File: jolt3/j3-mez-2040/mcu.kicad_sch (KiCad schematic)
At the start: 21 parts, among them SW2 SW_SPST, U1 RP2040, Y1 ABM8-272-T3

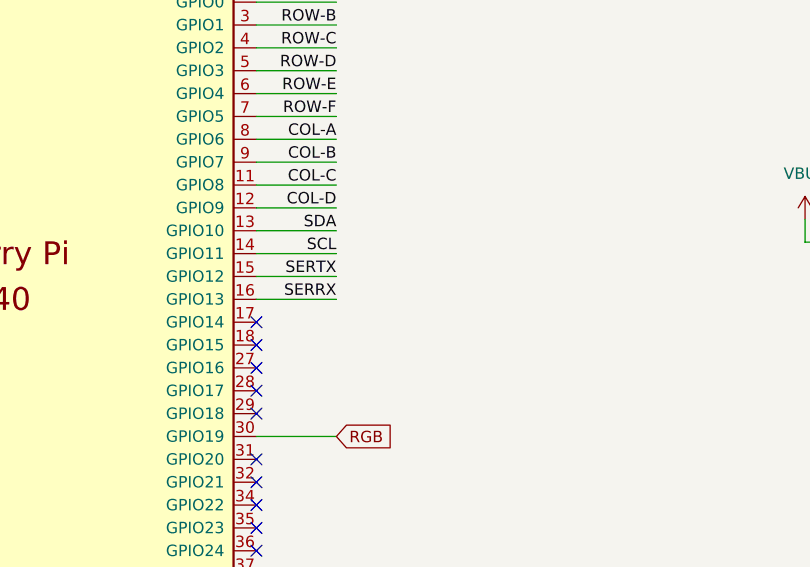
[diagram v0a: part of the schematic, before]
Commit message: Jolt 3: Rev A for 3 boards
Send Rev A out for jolt3-left, jolt3-right, and j3-mez-2040.
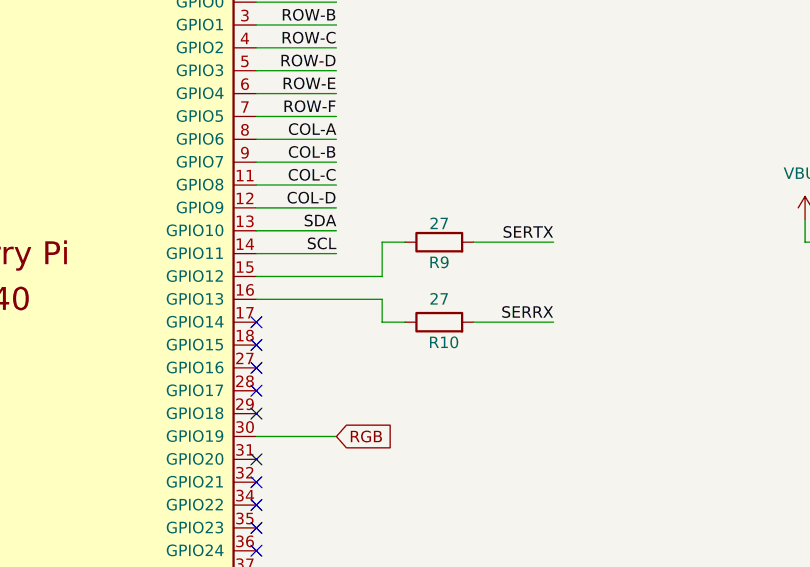
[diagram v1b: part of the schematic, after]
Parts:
- added R10, R9: 27, Resistor_SMD:R_0402_1005Metric, symbol Device:R
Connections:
- net SERRX: now also R10.2; no longer U1.16 (GPIO13)
- net SERTX: now also R9.2; no longer U1.15 (GPIO12)
- new net: R10.1, U1.16 (GPIO13)
- new net: R9.1, U1.15 (GPIO12)
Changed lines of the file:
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@@
+	(wire
+		(pts
+			(xy 146.05 134.62) (xy 148.59 134.62)
+		)
+		(stroke
+			(width 0)
+			(type default)
+		)
+	)
 	(wire
 		(pts
@@
 	(wire
 		(pts
-			(xy 132.08 138.43) (xy 140.97 138.43)
+			(xy 132.08 138.43) (xy 146.05 138.43)
 		)
 		(stroke
@@
 	(wire
 		(pts
+			(xy 146.05 143.51) (xy 148.59 143.51)
+		)
+		(stroke
+			(width 0)
+			(type default)
+		)
+	)
+	(wire
+		(pts
 			(xy 204.47 33.02) (xy 204.47 34.29)
 		)
@@
 	(wire
 		(pts
+			(xy 146.05 140.97) (xy 146.05 143.51)
+		)
+		(stroke
+			(width 0)
+			(type default)
+		)
+	)
+	(wire
+		(pts
 			(xy 116.84 33.02) (xy 116.84 52.07)
 		)
@@
 	(wire
 		(pts
+			(xy 146.05 138.43) (xy 146.05 134.62)
+		)
+		(stroke
+			(width 0)
+			(type default)
+		)
+	)
+	(wire
+		(pts
 			(xy 179.07 41.91) (xy 179.07 44.45)
 		)
@@
 	(wire
 		(pts
+			(xy 156.21 143.51) (xy 165.1 143.51)
+		)
+		(stroke
+			(width 0)
+			(type default)
+		)
+	)
+	(wire
+		(pts
 			(xy 116.84 63.5) (xy 116.84 90.17)
 		)
@@
 	(wire
 		(pts
-			(xy 132.08 140.97) (xy 140.97 140.97)
+			(xy 132.08 140.97) (xy 146.05 140.97)
 		)
 		(stroke
@@
 		(pts
 			(xy 132.08 113.03) (xy 140.97 113.03)
+		)
+		(stroke
+			(width 0)
+			(type default)
+		)
+	)
+	(wire
+		(pts
+			(xy 156.21 134.62) (xy 165.1 134.62)
 		)
 		(stroke
@@
 	)
 	(label "SERTX"
-		(at 140.97 138.43 180)
+		(at 165.1 134.62 180)
 		(effects
 			(font
@@
 	)
 	(label "SERRX"
-		(at 140.97 140.97 180)
+		(at 165.1 143.51 180)
 		(effects
 			(font
@@
 		)
 	)
+	(symbol
+		(lib_id "Device:R")
+		(at 152.4 143.51 90)
+		(unit 1)
+		(exclude_from_sim no)
+		(in_bom yes)
+		(on_board yes)
+		(dnp no)
+		(property "Reference" "R10"
+			(at 152.908 145.796 90)
+			(effects
+				(font
+					(size 1.27 1.27)
+				)
+			)
+		)
+		(property "Value" "27"
+			(at 152.4 140.97 90)
+			(effects
+				(font
+					(size 1.27 1.27)
+				)
+			)
+		)
+		(property "Footprint" "Resistor_SMD:R_0402_1005Metric"
+			(at 152.4 145.288 90)
+			(effects
+				(font
+					(size 1.27 1.27)
+				)
+				(hide yes)
+			)
+		)
+		(property "Datasheet" "~"
+			(at 152.4 143.51 0)
+			(effects
+				(font
+					(size 1.27 1.27)
+				)
+				(hide yes)
+			)
+		)
+		(property "Description" "Resistor"
+			(at 152.4 143.51 0)
+			(effects
+				(font
+					(size 1.27 1.27)
+				)
+				(hide yes)
+			)
+		)
+		(pin "2"
+		)
+		(pin "1"
+		)
+		(instances
+			(project "j3-mez-2040"
+				(path "/5e404b8e-7f18-4204-bb67-87c83d2db771/71e7df0f-b1c8-4404-9fb3-fe16e4220fb1"
+					(reference "R10")
+					(unit 1)
+				)
+			)
+		)
+	)
+	(symbol
+		(lib_id "Device:R")
+		(at 152.4 134.62 90)
+		(unit 1)
+		(exclude_from_sim no)
+		(in_bom yes)
+		(on_board yes)
+		(dnp no)
+		(property "Reference" "R9"
+			(at 152.4 136.906 90)
+			(effects
+				(font
+					(size 1.27 1.27)
+				)
+			)
+		)
+		(property "Value" "27"
+			(at 152.4 132.588 90)
+			(effects
+				(font
+					(size 1.27 1.27)
+				)
+			)
+		)
+		(property "Footprint" "Resistor_SMD:R_0402_1005Metric"
+			(at 152.4 136.398 90)
+			(effects
+				(font
+					(size 1.27 1.27)
+				)
+				(hide yes)
+			)
+		)
+		(property "Datasheet" "~"
+			(at 152.4 134.62 0)
+			(effects
+				(font
+					(size 1.27 1.27)
+				)
+				(hide yes)
+			)
+		)
+		(property "Description" "Resistor"
+			(at 152.4 134.62 0)
+			(effects
+				(font
+					(size 1.27 1.27)
+				)
+				(hide yes)
+			)
+		)
+		(pin "2"
+		)
+		(pin "1"
+		)
+		(instances
+			(project "j3-mez-2040"
+				(path "/5e404b8e-7f18-4204-bb67-87c83d2db771/71e7df0f-b1c8-4404-9fb3-fe16e4220fb1"
+					(reference "R9")
+					(unit 1)
+				)
+			)
+		)
+	)
